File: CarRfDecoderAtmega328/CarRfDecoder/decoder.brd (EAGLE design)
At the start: 98.7 x 80 mm, 45 parts, among them T1 BC847, T2 BC847, T3 IRLML6402, U2 RFM69CW, U3 MCP73831, U4 ATMEGA328P, U6 MIC5219 3.3V

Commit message: changes in the design
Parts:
- added C1, C5: 22pF, SparkFun-Capacitors:0805
- moved U3 3.45 mm to (6.86, 4.93)
- moved BATGND 2.67 mm to (2.64, 3.45)
- moved BAT+ 2.47 mm to (2.64, 5.69)
- moved T3 1.84 mm to (6.55, 4.11)
- moved R3 1.63 mm to (3.30, 8.53)
- moved R9 1.30 mm to (15.0, 15.9)
- moved C2 1.22 mm to (6.55, 1.57)
- moved T1 1.02 mm to (6.60, 15.7)
- moved R6 0.91 mm to (10.2, 13.1)
- moved MOTORGND 0.86 mm to (2.69, 12.8)
- moved R1 0.73 mm to (10.6, 3.81)
- moved LDR 0.64 mm to (2.69, 14.8)
- moved MOTOR 0.64 mm to (2.69, 14.8)
- moved T2 0.64 mm to (6.50, 8.43)
- moved SI 0.64 mm to (28.8, 19.2), turned to 0 degrees
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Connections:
- new net N$2: C1.2, U4.7
- new net N$4: C5.2, U4.8
- net GND: now also C1.1, C5.1
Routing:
- net AX1: track 11.4 -> 31.4 mm, vias 0 -> 2
- net A4: track 0.00 -> 15.7 mm, vias 0 -> 1
- net GND: track 120.4 -> 131.1 mm, vias 4 -> 5
- net SCK: track 15.7 -> 25.0 mm, vias 2 -> 1
- net N$10: track 43.8 -> 51.5 mm, vias 6 -> 4
- net N$9: track 18.0 -> 10.2 mm, vias 2 -> 0
- net D7: track 31.7 -> 24.0 mm
- net VCC: track 48.5 -> 56.0 mm, vias 5 -> 4
- net A0: track 25.7 -> 31.3 mm, vias 2 -> 3
- net N$4: track 0.00 -> 5.21 mm
- net N$2: track 0.00 -> 4.64 mm
- net N$3: track 16.7 -> 12.1 mm, vias 2 -> 0
- net N$14: track 23.0 -> 18.5 mm, vias 2 -> 0
- net AREF: track 17.9 -> 20.7 mm
- net N$15: track 23.8 -> 21.2 mm, vias 0 -> 2
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
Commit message: Ready boards.
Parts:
- added VJ, VJ1, XTAL, XTAL1: (no value), wirepad:SMD1,27-2,54
- moved BLINK-L 4.91 mm to (29.3, 9.86)
- moved BLINK-R 4.71 mm to (29.3, 8.03)
- moved BBRKLIGHT 4.11 mm to (29.3, 6.10)
- moved R8 0.61 mm to (27.1, 6.45)
- moved ABRKLIGHT 0.41 mm to (29.3, 4.32)
- moved SI 0.20 mm to (29.0, 19.2)
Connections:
- new net N$1: U2.2, VJ.1
- net N$2: now also XTAL.1
- net N$4: now also XTAL1.1
- net VCC: now also VJ1.1; no longer U2.2
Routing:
- net A0: track 31.3 -> 63.4 mm, vias 3 -> 2
- net GND: track 131.1 -> 153.9 mm, vias 5 -> 2
- net AX1: track 31.4 -> 11.7 mm
- net A5: track 33.1 -> 20.2 mm
- net A3: track 16.0 -> 27.3 mm, vias 1 -> 2
- net N$1: track 0.00 -> 10.6 mm
- net N$10: track 51.5 -> 61.4 mm, vias 4 -> 3
- net SCK: track 25.0 -> 15.7 mm, vias 1 -> 2
- net AREF: track 20.7 -> 13.9 mm, vias 2 -> 0
- net N$13: track 7.22 -> 2.85 mm
- net N$16: track 6.39 -> 2.12 mm
- net N$3: track 12.1 -> 15.9 mm, vias 0 -> 2
- net SS: track 18.1 -> 14.6 mm
- net N$2: track 4.64 -> 7.93 mm
- net N$4: track 5.21 -> 8.46 mm
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
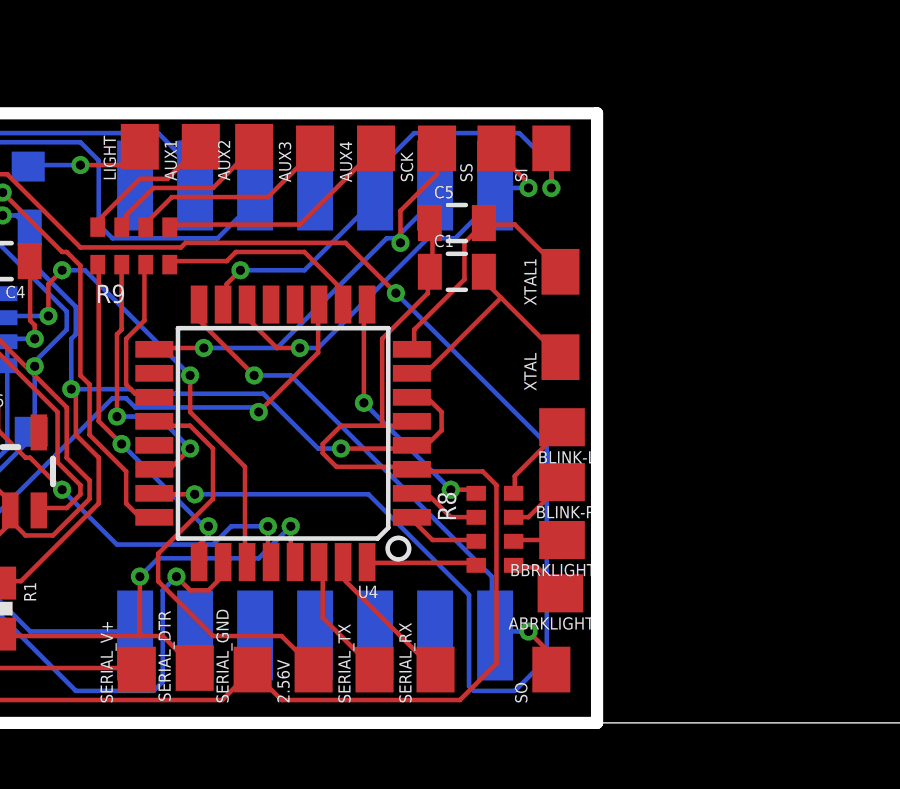
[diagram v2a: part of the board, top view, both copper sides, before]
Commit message: Fix connection to the rf module and add a 16mhz crystal
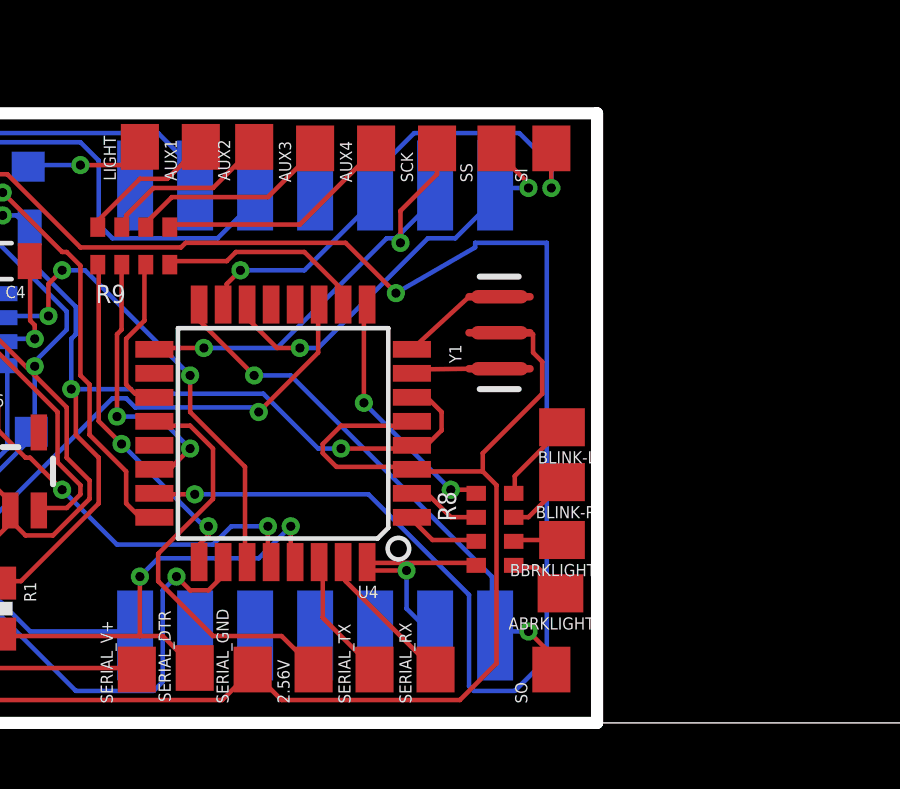
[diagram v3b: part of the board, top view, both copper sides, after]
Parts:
- removed C1, C5: 22pF, SparkFun-Capacitors:0805
- removed XTAL, XTAL1: (no value), wirepad:SMD1,27-2,54
- added Y1: 16MHZ, SparkFun-FreqCtrl:RESONATOR-SMD
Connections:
- net ABRKL: now also U2.9
- net GND: now also Y1.2; no longer C1.1, C5.1
- net N$2: now also Y1.1; no longer C1.2, XTAL.1
- net N$4: now also Y1.3; no longer C5.2, XTAL1.1
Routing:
- net N$2: track 7.93 -> 1.92 mm
- net N$4: track 8.46 -> 2.59 mm
- net A0: track 63.4 -> 68.6 mm
- net ABRKL: track 3.68 -> 7.81 mm, vias 0 -> 1
- net GND: track 153.9 -> 153.0 mm
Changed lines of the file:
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@@
 <element name="SCK" library="wirepad" package="SMD1,27-2,54" value="" x="25.146" y="19.1516"/>
 <element name="SERIAL_DTR" library="wirepad" package="SMD1,27-2,54" value="" x="17.0688" y="1.8288"/>
-<element name="C1" library="SparkFun-Capacitors" package="0805" value="22pF" x="25.8064" y="15.0368"/>
-<element name="C5" library="SparkFun-Capacitors" package="0805" value="22pF" x="25.8064" y="16.6624"/>
-<element name="XTAL" library="wirepad" package="SMD1,27-2,54" value="" x="29.2608" y="12.192"/>
-<element name="XTAL1" library="wirepad" package="SMD1,27-2,54" value="" x="29.2608" y="15.0368"/>
 <element name="VJ" library="wirepad" package="SMD1,27-2,54" value="" x="7.7216" y="19.1008" rot="MR0"/>
 <element name="VJ1" library="wirepad" package="SMD1,27-2,54" value="" x="4.6736" y="19.1008" rot="MR0"/>
+<element name="Y1" library="SparkFun-FreqCtrl" package="RESONATOR-SMD" value="16MHZ" x="27.2288" y="13.0048" rot="R90">
+<attribute name="PROD_ID" value="XTAL-08900" x="27.2288" y="13.0048" size="1.778" layer="27" rot="R90" display="off"/>
+</element>
 </elements>
 <signals>
@@
 <wire x1="9.906" y1="9.7536" x2="9.972" y2="9.6821" width="0.1524" layer="1"/>
 <wire x1="2.7432" y1="12.8016" x2="2.6924" y2="12.7" width="0.1524" layer="1"/>
-<wire x1="24.8412" y1="9.2964" x2="24.384" y2="9.2964" width="0.1524" layer="1"/>
-<wire x1="25.2984" y1="9.7536" x2="24.8412" y2="9.2964" width="0.1524" layer="1"/>
-<wire x1="25.2984" y1="10.3632" x2="25.2984" y2="9.7536" width="0.1524" layer="1"/>
-<wire x1="24.8412" y1="10.8204" x2="25.2984" y2="10.3632" width="0.1524" layer="1"/>
-<wire x1="24.384" y1="10.8204" x2="24.8412" y2="10.8204" width="0.1524" layer="1"/>
-<wire x1="24.384" y1="9.2964" x2="24.3078" y2="9.252" width="0.1524" layer="1"/>
-<wire x1="24.384" y1="10.8204" x2="24.3078" y2="10.852" width="0.1524" layer="1"/>
 <wire x1="11.2776" y1="4.7244" x2="10.668" y2="4.7244" width="0.1524" layer="1"/>
 <wire x1="13.8684" y1="7.3152" x2="11.2776" y2="4.7244" width="0.1524" layer="1"/>
@@
 <via x="5.0292" y="13.2588" extent="1-16" drill="0.3048"/>
 <via x="5.6388" y="16.3068" extent="1-16" drill="0.3048"/>
+<wire x1="24.8412" y1="10.8204" x2="24.384" y2="10.8204" width="0.1524" layer="1"/>
+<wire x1="25.2984" y1="10.3632" x2="24.8412" y2="10.8204" width="0.1524" layer="1"/>
+<wire x1="25.2984" y1="9.7536" x2="25.2984" y2="10.3632" width="0.1524" layer="1"/>
+<wire x1="24.8412" y1="9.2964" x2="25.2984" y2="9.7536" width="0.1524" layer="1"/>
+<wire x1="24.384" y1="9.2964" x2="24.8412" y2="9.2964" width="0.1524" layer="1"/>
+<wire x1="24.384" y1="10.8204" x2="24.3078" y2="10.852" width="0.1524" layer="1"/>
+<wire x1="24.384" y1="9.2964" x2="24.3078" y2="9.252" width="0.1524" layer="1"/>
 </signal>
 <signal name="GND">
@@
 <contactref element="U4" pad="3"/>
 <contactref element="SERIAL_GND" pad="1"/>
-<contactref element="C1" pad="1"/>
-<contactref element="C5" pad="1"/>
 <wire x1="11.7348" y1="12.0396" x2="11.7348" y2="11.8872" width="0.1524" layer="16"/>
 <wire x1="11.7348" y1="11.8872" x2="11.7348" y2="9.7536" width="0.1524" layer="16"/>
@@
 <wire x1="5.6388" y1="1.524" x2="5.6532" y2="1.5748" width="0.1524" layer="16"/>
 <wire x1="7.3152" y1="9.4488" x2="7.4524" y2="9.5328" width="0.1524" layer="16"/>
-<wire x1="24.9936" y1="16.6116" x2="24.9936" y2="15.0876" width="0.1524" layer="1"/>
-<wire x1="24.9936" y1="15.0876" x2="24.9064" y2="15.0368" width="0.1524" layer="1"/>
-<wire x1="24.9936" y1="16.6116" x2="24.9064" y2="16.6624" width="0.1524" layer="1"/>
-<wire x1="21.7932" y1="8.5344" x2="24.2316" y2="8.5344" width="0.1524" layer="1"/>
-<wire x1="21.336" y1="8.9916" x2="21.7932" y2="8.5344" width="0.1524" layer="1"/>
-<wire x1="21.336" y1="9.2964" x2="21.336" y2="8.9916" width="0.1524" layer="1"/>
-<wire x1="21.9456" y1="9.906" x2="21.336" y2="9.2964" width="0.1524" layer="1"/>
-<wire x1="24.2316" y1="9.906" x2="23.3172" y2="9.906" width="0.1524" layer="1"/>
-<wire x1="23.3172" y1="9.906" x2="21.9456" y2="9.906" width="0.1524" layer="1"/>
-<wire x1="24.2316" y1="8.5344" x2="24.3078" y2="8.452" width="0.1524" layer="1"/>
-<wire x1="24.2316" y1="9.906" x2="24.3078" y2="10.052" width="0.1524" layer="1"/>
-<wire x1="24.8412" y1="14.3256" x2="24.8412" y2="14.9352" width="0.1524" layer="1"/>
-<wire x1="23.3172" y1="12.8016" x2="24.8412" y2="14.3256" width="0.1524" layer="1"/>
-<wire x1="23.3172" y1="9.906" x2="23.3172" y2="12.8016" width="0.1524" layer="1"/>
-<wire x1="24.8412" y1="14.9352" x2="24.9064" y2="15.0368" width="0.1524" layer="1"/>
 <wire x1="6.5532" y1="3.2004" x2="6.858" y2="3.5052" width="0.1524" layer="1"/>
 <wire x1="6.5532" y1="3.048" x2="6.5532" y2="3.2004" width="0.1524" layer="1"/>
@@
 <via x="2.5908" y="2.286" extent="1-16" drill="0.3048"/>
 <via x="11.7348" y="11.8872" extent="1-16" drill="0.3048"/>
+<contactref element="Y1" pad="2"/>
+<wire x1="21.9456" y1="9.906" x2="24.2316" y2="9.906" width="0.1524" layer="1"/>
+<wire x1="21.336" y1="9.2964" x2="21.9456" y2="9.906" width="0.1524" layer="1"/>
+<wire x1="21.336" y1="8.9916" x2="21.336" y2="9.2964" width="0.1524" layer="1"/>
+<wire x1="21.7932" y1="8.5344" x2="21.336" y2="8.9916" width="0.1524" layer="1"/>
+<wire x1="24.2316" y1="8.5344" x2="21.7932" y2="8.5344" width="0.1524" layer="1"/>
+<wire x1="24.2316" y1="9.906" x2="24.3078" y2="10.052" width="0.1524" layer="1"/>
+<wire x1="24.2316" y1="8.5344" x2="24.3078" y2="8.452" width="0.1524" layer="1"/>
+<wire x1="28.3464" y1="12.3444" x2="28.3464" y2="12.954" width="0.1524" layer="1"/>
+<wire x1="28.6512" y1="12.0396" x2="28.3464" y2="12.3444" width="0.1524" layer="1"/>
+<wire x1="28.6512" y1="10.9728" x2="28.6512" y2="12.0396" width="0.1524" layer="1"/>
+<wire x1="26.67" y1="8.9916" x2="28.6512" y2="10.9728" width="0.1524" layer="1"/>
+<wire x1="26.67" y1="8.382" x2="26.67" y2="8.9916" width="0.1524" layer="1"/>
+<wire x1="28.3464" y1="12.954" x2="27.2288" y2="13.0048" width="0.1524" layer="1"/>
 </signal>
 <signal name="AREF">
@@
 <wire x1="27.7368" y1="1.0668" x2="26.3652" y2="1.0668" width="0.1524" layer="16"/>
 <wire x1="28.8036" y1="2.1336" x2="27.7368" y2="1.0668" width="0.1524" layer="16"/>
-<wire x1="28.8036" y1="9.2964" x2="28.8036" y2="2.1336" width="0.1524" layer="16"/>
-<wire x1="23.7744" y1="14.3256" x2="28.8036" y2="9.2964" width="0.1524" layer="16"/>
+<wire x1="28.8036" y1="16.002" x2="28.8036" y2="2.1336" width="0.1524" layer="16"/>
 <wire x1="22.098" y1="16.002" x2="23.7744" y2="14.3256" width="0.1524" layer="1"/>
 <wire x1="16.764" y1="16.002" x2="22.098" y2="16.002" width="0.1524" layer="1"/>
@@
 <via x="17.0688" y="7.62" extent="1-16" drill="0.3048"/>
 <via x="23.7744" y="14.3256" extent="1-16" drill="0.3048"/>
+<wire x1="28.8036" y1="16.002" x2="26.416" y2="16.002" width="0.1524" layer="16"/>
+<wire x1="26.416" y1="16.002" x2="26.416" y2="15.8496" width="0.1524" layer="16"/>
+<wire x1="26.416" y1="15.8496" x2="23.7744" y2="14.3256" width="0.1524" layer="16"/>
 </signal>
 <signal name="A1">
@@
 <wire x1="26.3652" y1="5.334" x2="26.4514" y2="5.2516" width="0.1524" layer="1"/>
 <wire x1="22.86" y1="5.334" x2="22.8152" y2="5.3594" width="0.1524" layer="1"/>
+<contactref element="U2" pad="9"/>
+<wire x1="24.13" y1="5.08" x2="22.86" y2="5.08" width="0.1524" layer="1"/>
+<wire x1="24.13" y1="3.81" x2="24.13" y2="5.08" width="0.1524" layer="16"/>
+<wire x1="24.765" y1="3.175" x2="24.13" y2="3.81" width="0.1524" layer="16"/>
+<wire x1="22.86" y1="5.08" x2="22.8152" y2="5.3594" width="0.1524" layer="1"/>
+<wire x1="24.765" y1="3.175" x2="25.082" y2="2.914" width="0.1524" layer="16"/>
+<via x="24.13" y="5.08" extent="1-16" drill="0.3048"/>
 </signal>
 <signal name="AX1">
@@
 </signal>
 <signal name="N$2">
-<contactref element="C1" pad="2"/>
 <contactref element="U4" pad="7"/>
-<contactref element="XTAL" pad="1"/>
-<wire x1="26.8224" y1="14.6304" x2="26.8224" y2="14.9352" width="0.1524" layer="1"/>
-<wire x1="29.2608" y1="12.192" x2="27.2796" y2="14.1732" width="0.1524" layer="1"/>
-<wire x1="27.2796" y1="14.1732" x2="26.8224" y2="14.6304" width="0.1524" layer="1"/>
-<wire x1="26.8224" y1="14.9352" x2="26.7064" y2="15.0368" width="0.1524" layer="1"/>
-<wire x1="24.8412" y1="11.7348" x2="24.384" y2="11.7348" width="0.1524" layer="1"/>
-<wire x1="27.2796" y1="14.1732" x2="24.8412" y2="11.7348" width="0.1524" layer="1"/>
-<wire x1="24.384" y1="11.7348" x2="24.3078" y2="11.652" width="0.1524" layer="1"/>
+<contactref element="Y1" pad="1"/>
+<wire x1="26.2128" y1="11.8048" x2="24.7904" y2="11.7856" width="0.1524" layer="1"/>
+<wire x1="24.7904" y1="11.7856" x2="24.3078" y2="11.652" width="0.1524" layer="1"/>
 </signal>
 <signal name="N$4">
-<contactref element="C5" pad="2"/>
 <contactref element="U4" pad="8"/>
-<contactref element="XTAL1" pad="1"/>
-<wire x1="27.7368" y1="16.6116" x2="26.8224" y2="16.6116" width="0.1524" layer="1"/>
-<wire x1="29.2608" y1="15.0876" x2="27.7368" y2="16.6116" width="0.1524" layer="1"/>
-<wire x1="26.8224" y1="16.6116" x2="26.7064" y2="16.6624" width="0.1524" layer="1"/>
-<wire x1="29.2608" y1="15.0876" x2="29.2608" y2="15.0368" width="0.1524" layer="1"/>
-<wire x1="24.384" y1="13.1064" x2="24.384" y2="12.4968" width="0.1524" layer="1"/>
-<wire x1="26.0604" y1="14.7828" x2="24.384" y2="13.1064" width="0.1524" layer="1"/>
-<wire x1="26.0604" y1="16.002" x2="26.0604" y2="14.7828" width="0.1524" layer="1"/>
-<wire x1="26.67" y1="16.6116" x2="26.0604" y2="16.002" width="0.1524" layer="1"/>
-<wire x1="24.384" y1="12.4968" x2="24.3078" y2="12.452" width="0.1524" layer="1"/>
-<wire x1="26.67" y1="16.6116" x2="26.7064" y2="16.6624" width="0.1524" layer="1"/>
+<contactref element="Y1" pad="3"/>
+<wire x1="26.2128" y1="14.2048" x2="24.3078" y2="12.452" width="0.1524" layer="1"/>
 </signal>
 <signal name="N$1">

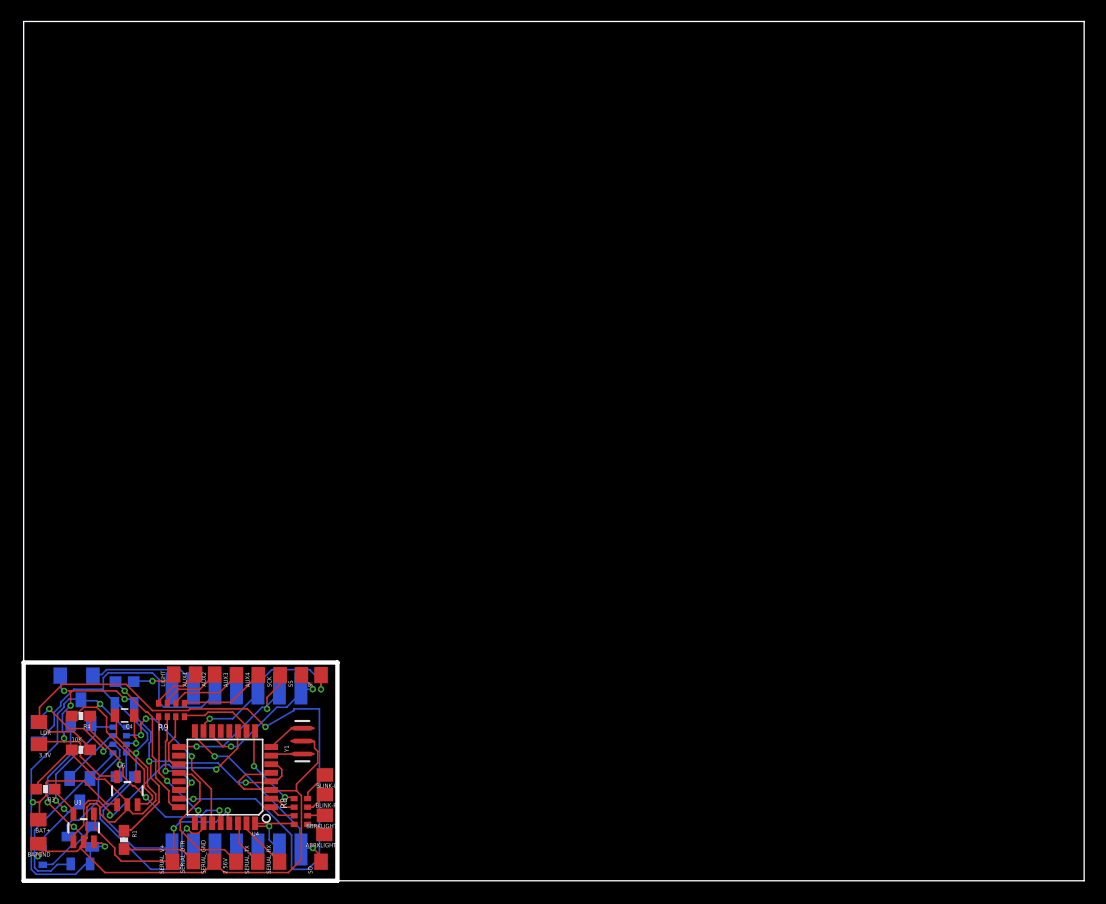
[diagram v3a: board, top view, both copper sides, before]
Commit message: Add gnd pad. Reduce the size
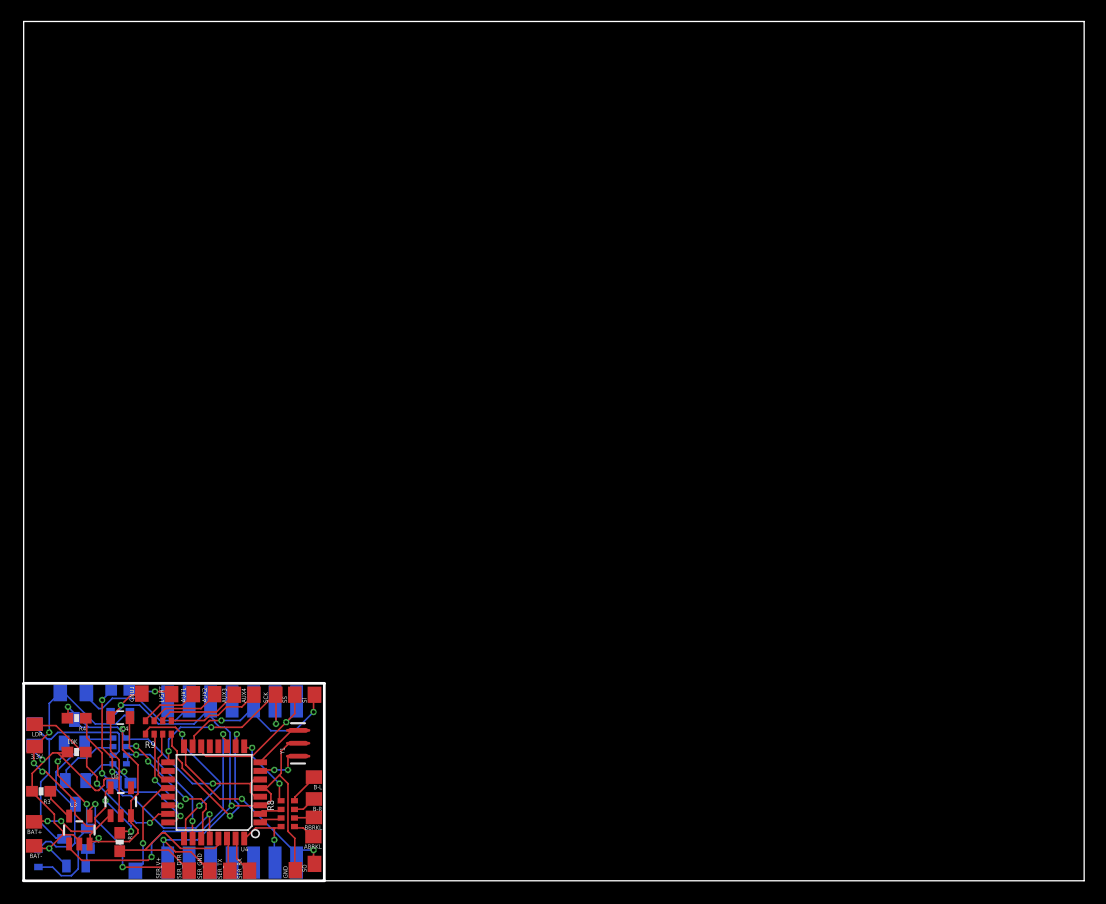
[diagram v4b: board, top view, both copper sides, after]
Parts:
- removed ABRKLIGHT, BATGND, BBRKLIGHT, BLINK-L, BLINK-R, SERIAL_DTR, SERIAL_GND, SERIAL_RX, SERIAL_TX, SERIAL_V+: (no value), wirepad:SMD1,27-2,54
- added ABRKL, B-L, B-R, BAT-, BBRKL, GND, GND1, SER_DTR, SER_GND, SER_RX, SER_TX, SER_V+: (no value), wirepad:SMD1,27-2,54
- moved 2.56V 9.40 mm to (11.7, 0.94), flipped to the bottom
- moved R9 2.03 mm to (13.8, 14.3)
- moved T1 1.93 mm to (5.99, 13.9)
- moved SI 1.93 mm to (28.3, 17.3)
- moved SS 1.93 mm to (26.5, 17.3)
- moved AUX4 1.87 mm to (22.7, 17.3)
- moved SCK 1.87 mm to (24.7, 17.3)
- moved AUX1 1.84 mm to (17.1, 17.4)
- moved LIGHT 1.84 mm to (15.0, 17.4)
- moved AUX3 1.84 mm to (20.9, 17.3)
- moved AUX2 1.83 mm to (19.1, 17.4)
- moved U4 1.75 mm to (19.0, 8.23)
- moved VJ 1.74 mm to (7.11, 17.5)
- moved VJ1 1.63 mm to (4.67, 17.5)
- moved U2 1.29 mm to (20.7, 9.19)
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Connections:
- removed net N$10: BAT+.1, C2.1, R4.2, R6.1, T1.3, T3.2, U3.3, U6.1, U6.3
- new net BAT+: BAT+.1, C2.1, R4.2, R6.1, T1.3, T3.2, U3.3, U4.4, U4.6, U6.1, U6.3
- net GND: now also BAT-.1, C3.1, GND.1, GND1.1, SER_GND.1; no longer BATGND.1, C3.2, SERIAL_GND.1
- net N$13: now also B-L.1; no longer BLINK-L.1
- net N$16: now also B-R.1; no longer BLINK-R.1
- net N$18: now also BBRKL.1; no longer BBRKLIGHT.1
- net N$20: now also ABRKL.1; no longer ABRKLIGHT.1
- net N$3: now also SER_DTR.1; no longer SERIAL_DTR.1
- net N$9: now also SER_V+.1; no longer SERIAL_V+.1
- net RX: now also SER_TX.1; no longer SERIAL_TX.1
- net TX: now also SER_RX.1; no longer SERIAL_RX.1
- net VCC: now also C3.2; no longer C3.1, U4.4, U4.6
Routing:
- net N$10: track 61.4 -> 0.00 mm, vias 3 -> 0
- net BAT+: track 0.00 -> 54.6 mm, vias 0 -> 6
- net A0: track 68.6 -> 17.7 mm
- net GND: track 153.0 -> 107.6 mm, vias 2 -> 6
- net VCC: track 53.0 -> 33.6 mm, vias 6 -> 5
- net AX4: track 6.97 -> 19.2 mm, vias 0 -> 2
- net A3: track 27.3 -> 16.3 mm
- net AX1: track 11.7 -> 16.7 mm
- net AREF: track 13.9 -> 9.28 mm, vias 0 -> 1
- net A1: track 14.5 -> 18.5 mm, vias 1 -> 3
- net SCK: track 15.7 -> 18.7 mm, vias 2 -> 3
- net N$2: track 1.92 -> 4.86 mm, vias 0 -> 2
- net D7: track 23.6 -> 26.2 mm
- net A4: track 15.8 -> 13.3 mm
- net N$9: track 10.2 -> 12.7 mm, vias 0 -> 2
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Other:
- outline, holes or cut-outs redrawn
- board text added: "3.3"
- board text removed: "3.3v"
